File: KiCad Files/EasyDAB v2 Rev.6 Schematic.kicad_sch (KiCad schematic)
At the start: 171 parts, among them IC1 CY7C1019DV33-10ZXCI, IC10 MP2307, IC11 MP2307, IC12 LD117AS33TR, IC2 M25P16, IC5 LD117A?S, IC6 LD117AS12TR, IC7 SPF5189Z, IC8 23LC1024 (optional), IC9 23LC1024 (optional)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

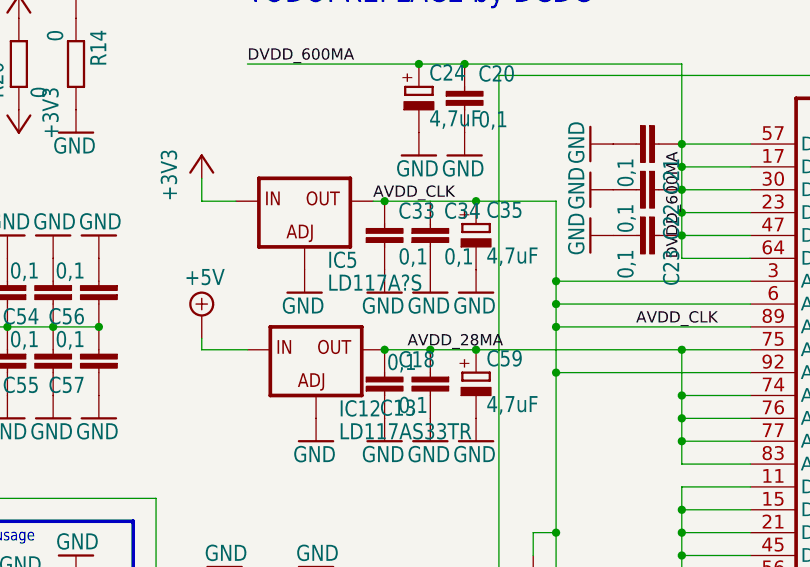
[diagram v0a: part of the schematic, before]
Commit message: Adding Correct Value for IC5
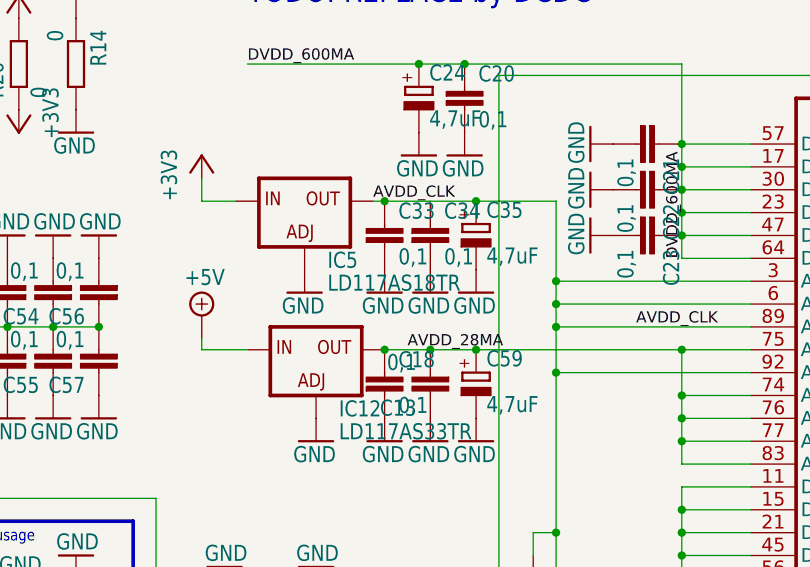
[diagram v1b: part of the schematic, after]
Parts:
- IC5: value LD117A?S -> LD117AS18TR
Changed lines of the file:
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@@
 			)
 		)
-		(property "Value" "LD117A?S"
+		(property "Value" "LD117AS18TR"
 			(at 392.43 54.61 0)
 			(effects
